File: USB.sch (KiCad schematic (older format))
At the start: 8 parts, among them J12 USB_B_Micro, U13 CP2102N-A01-GQFN24

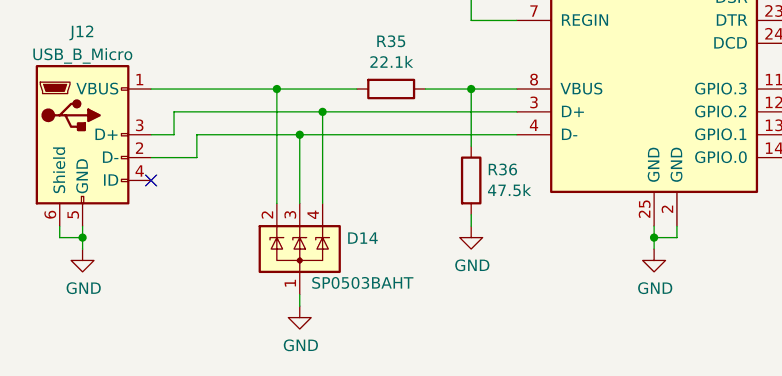
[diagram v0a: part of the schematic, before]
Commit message: Moves BAS70-04 to utsvt-chips because other systems use this component
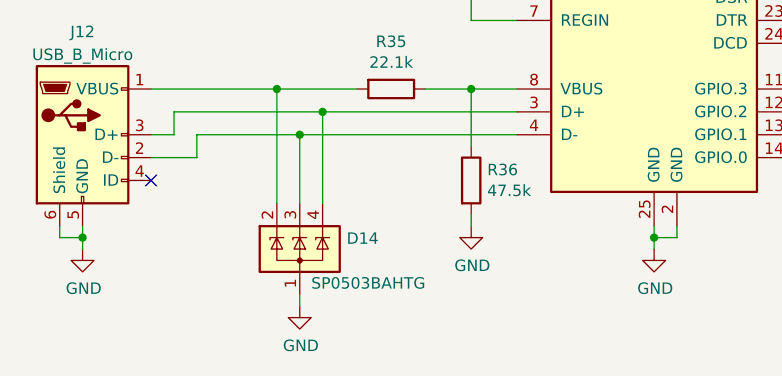
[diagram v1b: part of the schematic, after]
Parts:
- D14: value SP0503BAHT -> SP0503BAHTG
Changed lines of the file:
@@
 P 3950 4800
 F 0 "D14" H 4155 4846 50  0000 L CNN
-F 1 "SP0503BAHT" H 4000 4650 50  0000 L CNN
+F 1 "SP0503BAHTG" H 4000 4650 50  0000 L CNN
 F 2 "Package_TO_SOT_SMD:SOT-143" H 4175 4750 50  0001 L CNN
 F 3 "http://www.littelfuse.com/~/media/files/littelfuse/technical%20resources/documents/data%20sheets/sp05xxba.pdf" H 4075 4925 50  0001 C CNN

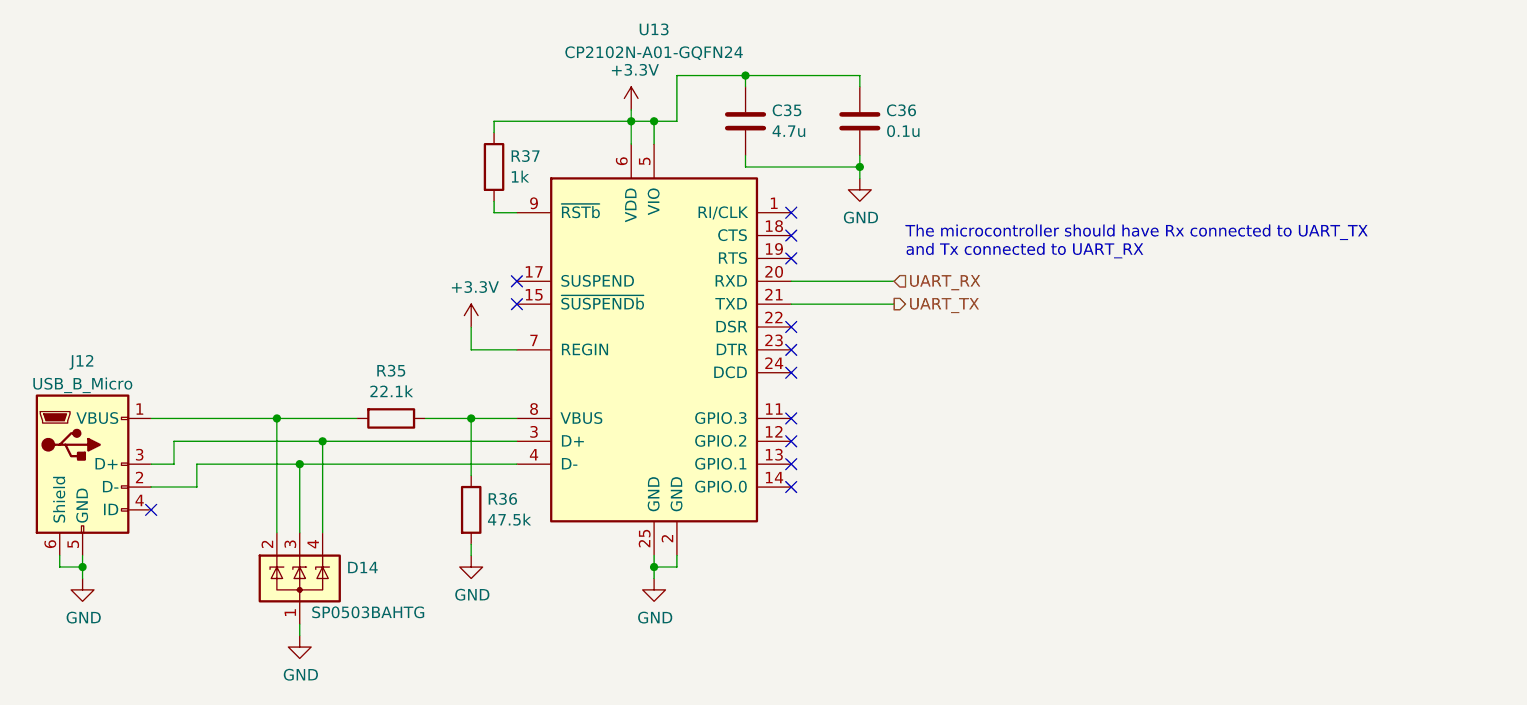
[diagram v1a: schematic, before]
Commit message: Updates BAS70-04 footprint for Contactor auxillary interface
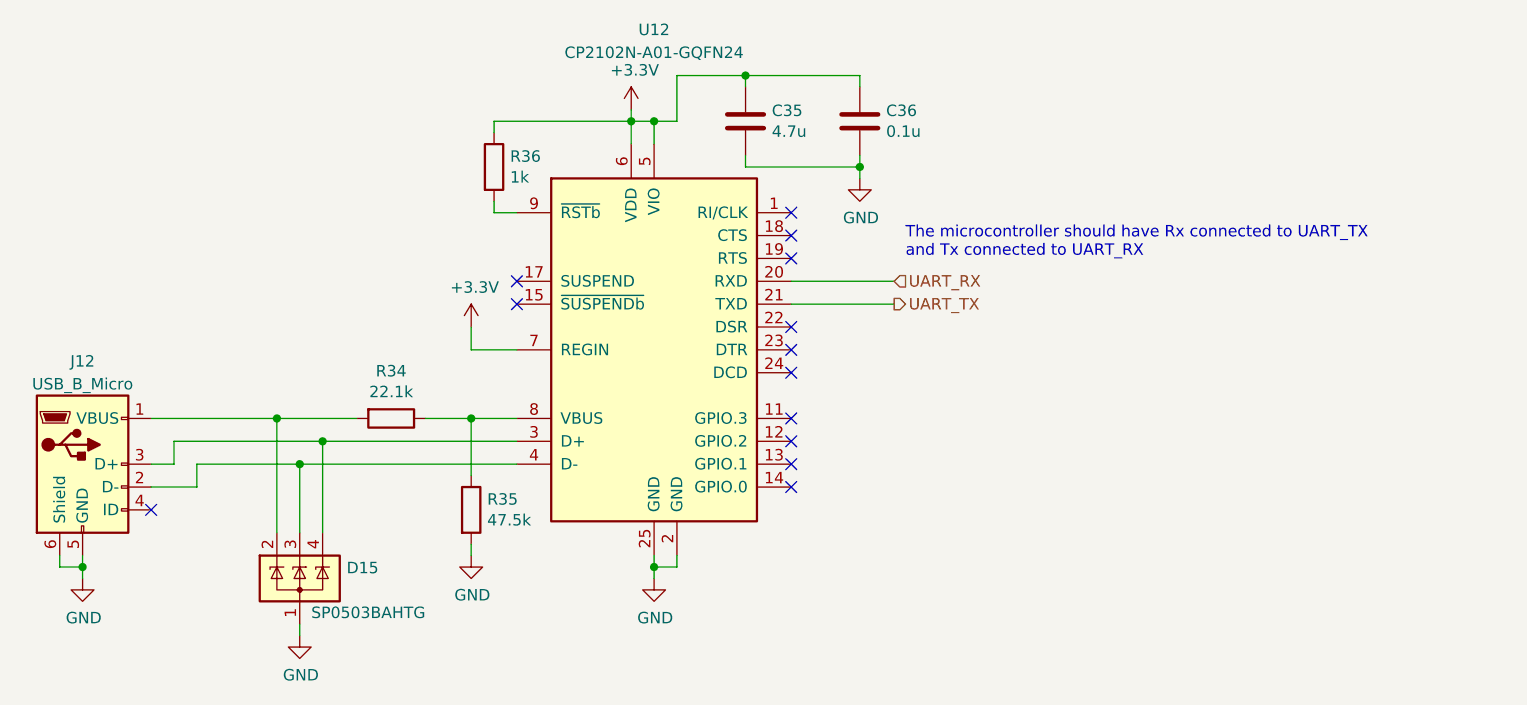
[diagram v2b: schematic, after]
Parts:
- renumbered D14 to D15, R35 to R34, R36 to R35, R37 to R36, U13 to U12
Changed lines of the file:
@@
 $EndDescr
 $Comp
-L Interface_USB:CP2102N-A01-GQFN24 U13
+L Interface_USB:CP2102N-A01-GQFN24 U12
 U 1 1 5C4963B2
 P 5500 3800
-F 0 "U13" H 5500 5200 50  0000 C CNN
+F 0 "U12" H 5500 5200 50  0000 C CNN
 F 1 "CP2102N-A01-GQFN24" H 5500 5100 50  0000 C CNN
 F 2 "Package_DFN_QFN:QFN-24-1EP_4x4mm_P0.5mm_EP2.6x2.6mm" H 5950 3000 50  0001 L CNN
@@
 	3500 4400 3500 4300
 $Comp
-L power:GND #PWR073
+L power:GND #PWR075
 U 1 1 5C4965DF
 P 3000 4800
-F 0 "#PWR073" H 3000 4550 50  0001 C CNN
+F 0 "#PWR075" H 3000 4550 50  0001 C CNN
 F 1 "GND" H 3005 4627 50  0000 C CNN
 F 2 "" H 3000 4800 50  0001 C CNN
@@
 Connection ~ 3000 4750
 $Comp
-L power:GND #PWR078
+L power:GND #PWR080
 U 1 1 5C4966CF
 P 5500 4800
-F 0 "#PWR078" H 5500 4550 50  0001 C CNN
+F 0 "#PWR080" H 5500 4550 50  0001 C CNN
 F 1 "GND" H 5505 4627 50  0000 C CNN
 F 2 "" H 5500 4800 50  0001 C CNN
@@
 	5500 4750 5500 4800
 $Comp
-L Power_Protection:SP0503BAHT D14
+L Power_Protection:SP0503BAHT D15
 U 1 1 5C496C9B
 P 3950 4800
-F 0 "D14" H 4155 4846 50  0000 L CNN
+F 0 "D15" H 4155 4846 50  0000 L CNN
 F 1 "SP0503BAHTG" H 4000 4650 50  0000 L CNN
 F 2 "Package_TO_SOT_SMD:SOT-143" H 4175 4750 50  0001 L CNN
@@
 $EndComp
 $Comp
-L power:GND #PWR074
+L power:GND #PWR076
 U 1 1 5C497074
 P 3950 5050
-F 0 "#PWR074" H 3950 4800 50  0001 C CNN
+F 0 "#PWR076" H 3950 4800 50  0001 C CNN
 F 1 "GND" H 3955 4877 50  0000 C CNN
 F 2 "" H 3950 5050 50  0001 C CNN
@@
 	3850 4600 3850 4100
 $Comp
-L Device:R R36
+L Device:R R35
 U 1 1 5C497DB9
 P 4700 4500
-F 0 "R36" H 4770 4546 50  0000 L CNN
+F 0 "R35" H 4770 4546 50  0000 L CNN
 F 1 "47.5k" H 4770 4455 50  0000 L CNN
 F 2 "Resistor_SMD:R_0805_2012Metric" V 4630 4500 50  0001 C CNN
@@
 $EndComp
 $Comp
-L Device:R R35
+L Device:R R34
 U 1 1 5C497DDB
 P 4350 4100
-F 0 "R35" V 4143 4100 50  0000 C CNN
+F 0 "R34" V 4143 4100 50  0000 C CNN
 F 1 "22.1k" V 4234 4100 50  0000 C CNN
 F 2 "Resistor_SMD:R_0805_2012Metric" V 4280 4100 50  0001 C CNN
@@
 	4200 4100 3850 4100
 $Comp
-L power:GND #PWR076
+L power:GND #PWR078
 U 1 1 5C498DBE
 P 4700 4700
-F 0 "#PWR076" H 4700 4450 50  0001 C CNN
+F 0 "#PWR078" H 4700 4450 50  0001 C CNN
 F 1 "GND" H 4705 4527 50  0000 C CNN
 F 2 "" H 4700 4700 50  0001 C CNN
@@
 	4700 4700 4700 4650
 $Comp
-L power:+3.3V #PWR077
+L power:+3.3V #PWR079
 U 1 1 5C499E7D
 P 5400 2750
-F 0 "#PWR077" H 5400 2600 50  0001 C CNN
+F 0 "#PWR079" H 5400 2600 50  0001 C CNN
 F 1 "+3.3V" H 5415 2923 50  0000 C CNN
 F 2 "" H 5400 2750 50  0001 C CNN
@@
 Connection ~ 5400 2800
 $Comp
-L Device:R R37
+L Device:R R36
 U 1 1 5C49B01B
 P 4800 3000
-F 0 "R37" H 4870 3046 50  0000 L CNN
+F 0 "R36" H 4870 3046 50  0000 L CNN
 F 1 "1k" H 4870 2955 50  0000 L CNN
 F 2 "Resistor_SMD:R_0805_2012Metric" V 4730 3000 50  0001 C CNN
@@
 NoConn ~ 6100 4400
 $Comp
-L power:+3.3V #PWR075
+L power:+3.3V #PWR077
 U 1 1 5C4A2CBF
 P 4700 3700
-F 0 "#PWR075" H 4700 3550 50  0001 C CNN
+F 0 "#PWR077" H 4700 3550 50  0001 C CNN
 F 1 "+3.3V" H 4715 3873 50  0000 C CNN
 F 2 "" H 4700 3700 50  0001 C CNN
@@
 $EndComp
 $Comp
-L power:GND #PWR079
+L power:GND #PWR081
 U 1 1 5C4A4BE4
 P 6400 3050
-F 0 "#PWR079" H 6400 2800 50  0001 C CNN
+F 0 "#PWR081" H 6400 2800 50  0001 C CNN
 F 1 "GND" H 6405 2877 50  0000 C CNN
 F 2 "" H 6400 3050 50  0001 C CNN
